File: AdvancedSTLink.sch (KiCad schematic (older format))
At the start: 56 parts, among them J1 USB_C_Receptacle, J2 Conn_02x03_Odd_Even, J3 Conn_01x06, J4 Conn_02x03_Odd_Even, Q1 S8050, SW1 SW_SPDT, U1 STM32F205RETx, U2 XC6206P332MR, U3 USBLC6-2P6, U4 MP2359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

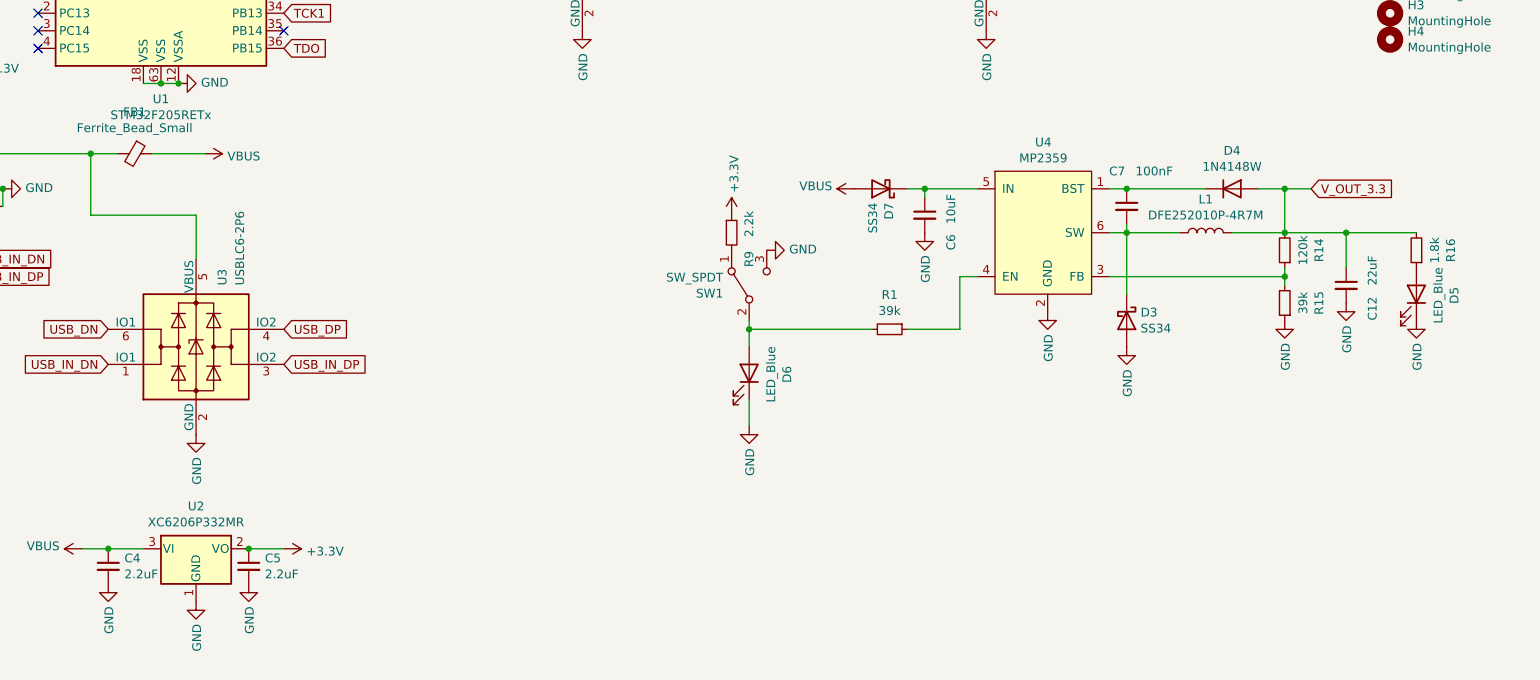
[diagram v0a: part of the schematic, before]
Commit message: Change DCDC design.
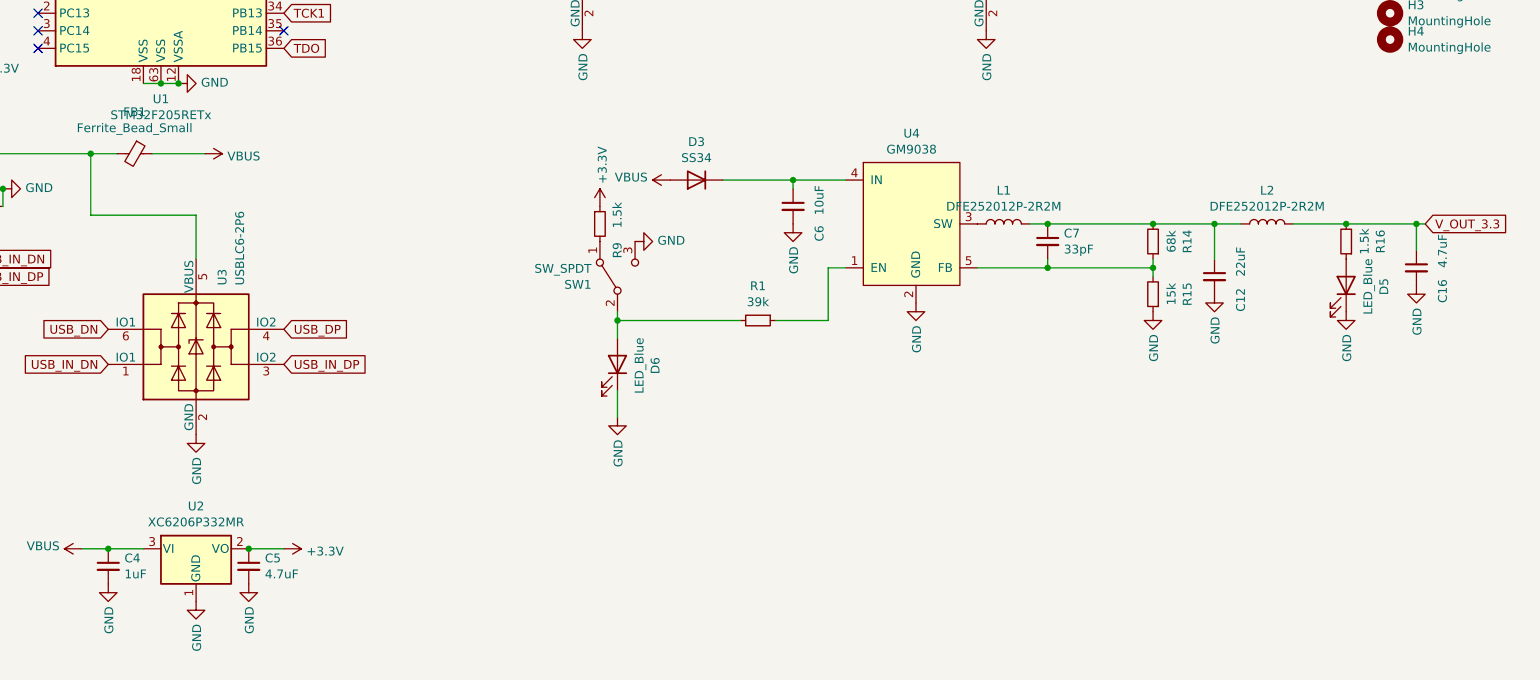
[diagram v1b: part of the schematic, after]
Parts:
- removed D3, D7: SS34, lc:SMA(DO-214AC)_S1, symbol Diode:B230
- removed D4: 1N4148W, lc:SOD-323, symbol Diode:1N4148W
- removed U4: MP2359, lc:SOT-23-6, symbol MP2359:MP2359
- added C16: 4.7uF, Capacitor_SMD:C_0603_1608Metric, symbol Device:C_Small
- added D3: SS34, lc:SMA(DO-214AC)_S1, symbol Device:D
- added L2: DFE252012P-2R2M, Inductor_SMD:L_TDK_NLV25_2.5x2.0mm, symbol Device:L
- added U4: GM9038, lc:SOT-23-5, symbol MP2359:GM9038
- C4: value 2.2uF -> 1uF
- C5: value 2.2uF -> 4.7uF; footprint Capacitor_SMD:C_0402_1005Metric -> Capacitor_SMD:C_0603_1608Metric
- C7: value 100nF -> 33pF
- L1: value DFE252010P-4R7M -> DFE252012P-2R2M
- R14: value 120k -> 68k
- R15: value 39k -> 15k
- R16: value 1.8k -> 1.5k
- R9: value 2.2k -> 1.5k
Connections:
- net GND: now also C16.2, U4.2 (GND)
- net VBUS: now also D3.2 (A)
- net V_OUT_3.3: now also C16.1, L2.2; no longer C12.1, L1.2, R14.2
- net at C7.1: now also C12.1, L1.2, R14.2, L2.1
- net at R14.1, R15.2: now also C7.2, U4.5 (FB)
- net at R1.1: now also U4.1 (EN)
- net at C6.1: now also D3.1 (K), U4.4 (IN)
- net at L1.1: now also U4.3 (SW); no longer C7.2
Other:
- moved on the sheet: C12, C6, D5, D6, L1, R1, R14, R15, R16, R9, SW1

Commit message: Layout.
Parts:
- added C17: 10uF, Capacitor_SMD:C_0603_1608Metric, symbol Device:C_Small
- added H? (x2): MouseBite, mouse_bite:mouse-bite-3mm-slot, symbol Mechanical:MountingHole
- C12: value 22uF -> 10uF
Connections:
- net GND: now also C17.2
- net at C12.1, C7.1, L1.2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: now also C17.1
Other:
- moved on the sheet: L2
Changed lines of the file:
@@
 L power:GND #PWR032
 U 1 1 5EA541D1
-P 8450 5800
-F 0 "#PWR032" H 8450 5550 50  0001 C CNN
-F 1 "GND" V 8455 5672 50  0000 R CNN
-F 2 "" H 8450 5800 50  0001 C CNN
-F 3 "" H 8450 5800 50  0001 C CNN
-	1    8450 5800
+P 8450 5900
+F 0 "#PWR032" H 8450 5650 50  0001 C CNN
+F 1 "GND" V 8455 5772 50  0000 R CNN
+F 2 "" H 8450 5900 50  0001 C CNN
+F 3 "" H 8450 5900 50  0001 C CNN
+	1    8450 5900
 	1    0    0    -1
 $EndComp
@@
 P 8800 5600
 F 0 "C12" V 8950 5400 50  0000 L CNN
-F 1 "22uF" V 8950 5600 50  0000 L CNN
+F 1 "10uF" V 8950 5600 50  0000 L CNN
 F 2 "Capacitor_SMD:C_0603_1608Metric" H 8800 5600 50  0001 C CNN
 F 3 "~" H 8800 5600 50  0001 C CNN
@@
 L power:GND #PWR051
 U 1 1 5EA99BA7
-P 8800 5700
-F 0 "#PWR051" H 8800 5450 50  0001 C CNN
-F 1 "GND" V 8805 5572 50  0000 R CNN
-F 2 "" H 8800 5700 50  0001 C CNN
-F 3 "" H 8800 5700 50  0001 C CNN
-	1    8800 5700
+P 8800 5900
+F 0 "#PWR051" H 8800 5650 50  0001 C CNN
+F 1 "GND" V 8805 5772 50  0000 R CNN
+F 2 "" H 8800 5900 50  0001 C CNN
+F 3 "" H 8800 5900 50  0001 C CNN
+	1    8800 5900
 	1    0    0    -1
 $EndComp
@@
 L Device:L L2
 U 1 1 5EE835EA
-P 9100 5300
-F 0 "L2" V 9290 5300 50  0000 C CNN
-F 1 "DFE252012P-2R2M" V 9199 5300 50  0000 C CNN
-F 2 "Inductor_SMD:L_TDK_NLV25_2.5x2.0mm" H 9100 5300 50  0001 C CNN
-F 3 "https://www.murata.com/~/media/webrenewal/products/inductor/chip/tokoproducts/wirewoundmetalalloychiptype/m_dfe252010p.ashx" H 9100 5300 50  0001 C CNN
-	1    9100 5300
+P 9400 5300
+F 0 "L2" V 9590 5300 50  0000 C CNN
+F 1 "DFE252012P-2R2M" V 9499 5300 50  0000 C CNN
+F 2 "Inductor_SMD:L_TDK_NLV25_2.5x2.0mm" H 9400 5300 50  0001 C CNN
+F 3 "https://www.murata.com/~/media/webrenewal/products/inductor/chip/tokoproducts/wirewoundmetalalloychiptype/m_dfe252010p.ashx" H 9400 5300 50  0001 C CNN
+	1    9400 5300
 	0    -1   -1   0
 $EndComp
@@
 Wire Wire Line
 	7850 5550 8450 5550
-Wire Wire Line
-	8800 5300 8950 5300
 Connection ~ 8800 5300
 Wire Wire Line
-	9250 5300 9550 5300
+	9550 5300 9950 5300
 Connection ~ 9550 5300
-Wire Wire Line
-	9550 5300 9950 5300
+$Comp
+L Device:C_Small C17
+U 1 1 5EEFBFCA
+P 9100 5600
+F 0 "C17" V 9250 5400 50  0000 L CNN
+F 1 "10uF" V 9250 5600 50  0000 L CNN
+F 2 "Capacitor_SMD:C_0603_1608Metric" H 9100 5600 50  0001 C CNN
+F 3 "~" H 9100 5600 50  0001 C CNN
+	1    9100 5600
+	1    0    0    -1
+$EndComp
+Wire Wire Line
+	8450 5900 8450 5800
+Wire Wire Line
+	8800 5700 8800 5850
+Wire Wire Line
+	9100 5700 9100 5850
+Wire Wire Line
+	9100 5850 8800 5850
+Connection ~ 8800 5850
+Wire Wire Line
+	8800 5850 8800 5900
+Wire Wire Line
+	8800 5300 9100 5300
+Wire Wire Line
+	9100 5500 9100 5300
+Connection ~ 9100 5300
+Wire Wire Line
+	9100 5300 9250 5300
+$Comp
+L Mechanical:MountingHole H?
+U 1 1 5EF396E4
+P 9800 4700
+F 0 "H?" H 9900 4746 50  0000 L CNN
+F 1 "MouseBite" H 9900 4655 50  0000 L CNN
+F 2 "mouse_bite:mouse-bite-3mm-slot" H 9800 4700 50  0001 C CNN
+F 3 "~" H 9800 4700 50  0001 C CNN
+	1    9800 4700
+	1    0    0    -1
+$EndComp
+$Comp
+L Mechanical:MountingHole H?
+U 1 1 5EF3A2E2
+P 9800 4900
+F 0 "H?" H 9900 4946 50  0000 L CNN
+F 1 "MouseBite" H 9900 4855 50  0000 L CNN
+F 2 "mouse_bite:mouse-bite-3mm-slot" H 9800 4900 50  0001 C CNN
+F 3 "~" H 9800 4900 50  0001 C CNN
+	1    9800 4900
+	1    0    0    -1
+$EndComp
 $EndSCHEMATC

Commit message: Layout optimizations.
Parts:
- added C18: 100nF, Capacitor_SMD:C_0402_1005Metric, symbol Device:C_Small
- D5: value LED_Blue -> LED_Green
- R16: value 1.5k -> 2.2k
- gave numbers to parts that had none: 2
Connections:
- net +3V3: now also C18.1
- net GND: now also C18.2
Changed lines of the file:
@@
 P 9550 5650
 F 0 "D5" H 9543 5866 50  0000 C CNN
-F 1 "LED_Blue" H 9543 5775 50  0000 C CNN
+F 1 "LED_Green" H 9543 5775 50  0000 C CNN
 F 2 "LED_SMD:LED_0603_1608Metric_Pad1.05x0.95mm_HandSolder" H 9550 5650 50  0001 C CNN
 F 3 "~" H 9550 5650 50  0001 C CNN
@@
 P 9550 5400
 F 0 "R16" V 9354 5400 50  0000 C CNN
-F 1 "1.5k" V 9445 5400 50  0000 C CNN
+F 1 "2.2k" V 9445 5400 50  0000 C CNN
 F 2 "Resistor_SMD:R_0402_1005Metric" H 9550 5400 50  0001 C CNN
 F 3 "~" H 9550 5400 50  0001 C CNN
@@
 	9100 5300 9250 5300
 $Comp
-L Mechanical:MountingHole H?
+L Mechanical:MountingHole H5
 U 1 1 5EF396E4
 P 9800 4700
-F 0 "H?" H 9900 4746 50  0000 L CNN
+F 0 "H5" H 9900 4746 50  0000 L CNN
 F 1 "MouseBite" H 9900 4655 50  0000 L CNN
 F 2 "mouse_bite:mouse-bite-3mm-slot" H 9800 4700 50  0001 C CNN
@@
 $EndComp
 $Comp
-L Mechanical:MountingHole H?
+L Mechanical:MountingHole H6
 U 1 1 5EF3A2E2
 P 9800 4900
-F 0 "H?" H 9900 4946 50  0000 L CNN
+F 0 "H6" H 9900 4946 50  0000 L CNN
 F 1 "MouseBite" H 9900 4855 50  0000 L CNN
 F 2 "mouse_bite:mouse-bite-3mm-slot" H 9800 4900 50  0001 C CNN
@@
 	1    0    0    -1
 $EndComp
+$Comp
+L power:+3.3V #PWR0116
+U 1 1 5EF48E60
+P 5700 1000
+F 0 "#PWR0116" H 5700 850 50  0001 C CNN
+F 1 "+3.3V" V 5715 1128 50  0000 L CNN
+F 2 "" H 5700 1000 50  0001 C CNN
+F 3 "" H 5700 1000 50  0001 C CNN
+	1    5700 1000
+	1    0    0    -1
+$EndComp
+$Comp
+L Device:C_Small C18
+U 1 1 5EF48E66
+P 5700 1100
+F 0 "C18" H 5792 1146 50  0000 L CNN
+F 1 "100nF" H 5792 1055 50  0000 L CNN
+F 2 "Capacitor_SMD:C_0402_1005Metric" H 5700 1100 50  0001 C CNN
+F 3 "~" H 5700 1100 50  0001 C CNN
+	1    5700 1100
+	1    0    0    -1
+$EndComp
+$Comp
+L power:GND #PWR0117
+U 1 1 5EF48E6C
+P 5700 1200
+F 0 "#PWR0117" H 5700 950 50  0001 C CNN
+F 1 "GND" H 5705 1027 50  0000 C CNN
+F 2 "" H 5700 1200 50  0001 C CNN
+F 3 "" H 5700 1200 50  0001 C CNN
+	1    5700 1200
+	1    0    0    -1
+$EndComp

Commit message: Fixes.
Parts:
- FB1: footprint Inductor_SMD:L_0603_1608Metric -> Inductor_SMD:L_0805_2012Metric
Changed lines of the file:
@@
 F 0 "FB1" V 2413 4900 50  0000 C CNN
 F 1 "Ferrite_Bead_Small" V 2504 4900 50  0000 C CNN
-F 2 "Inductor_SMD:L_0603_1608Metric" V 2580 4900 50  0001 C CNN
+F 2 "Inductor_SMD:L_0805_2012Metric" V 2580 4900 50  0001 C CNN
 F 3 "~" H 2650 4900 50  0001 C CNN
 	1    2650 4900

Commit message: Move ESD.
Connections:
- net USB_DN: now also U3.3 (IO2); no longer U3.6 (IO1)
- net USB_DP: now also U3.1 (IO1); no longer U3.4 (IO2)
- net USB_IN_DN: now also U3.4 (IO2); no longer U3.1 (IO1)
- net USB_IN_DP: now also U3.6 (IO1); no longer U3.3 (IO2)
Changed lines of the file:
@@
 	1    0    0    -1
 $EndComp
-Text GLabel 2500 5900 0    50   Input ~ 0
+Text GLabel 2500 6100 0    50   Input ~ 0
+USB_DP
+Text GLabel 3500 6100 2    50   Input ~ 0
 USB_DN
-Text GLabel 3500 5900 2    50   Input ~ 0
-USB_DP
 $Comp
 L power:GND #PWR019
@@
 	1    0    0    -1
 $EndComp
-Text GLabel 3500 6100 2    50   Input ~ 0
+Text GLabel 3500 5900 2    50   Input ~ 0
+USB_IN_DN
+Text GLabel 2500 5900 0    50   Input ~ 0
 USB_IN_DP
-Text GLabel 2500 6100 0    50   Input ~ 0
-USB_IN_DN
 Text GLabel 1700 5600 2    50   Input ~ 0
 USB_IN_DP
